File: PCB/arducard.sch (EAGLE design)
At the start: 54 parts, among them J1 USB MICRO, Q1 BC817-16LT1SMD, Q2 NTR0202PL, U1 microSD, U2 ATMEGA32U4-XUAU, U3 LM3658, Y1 16MHz KX-7

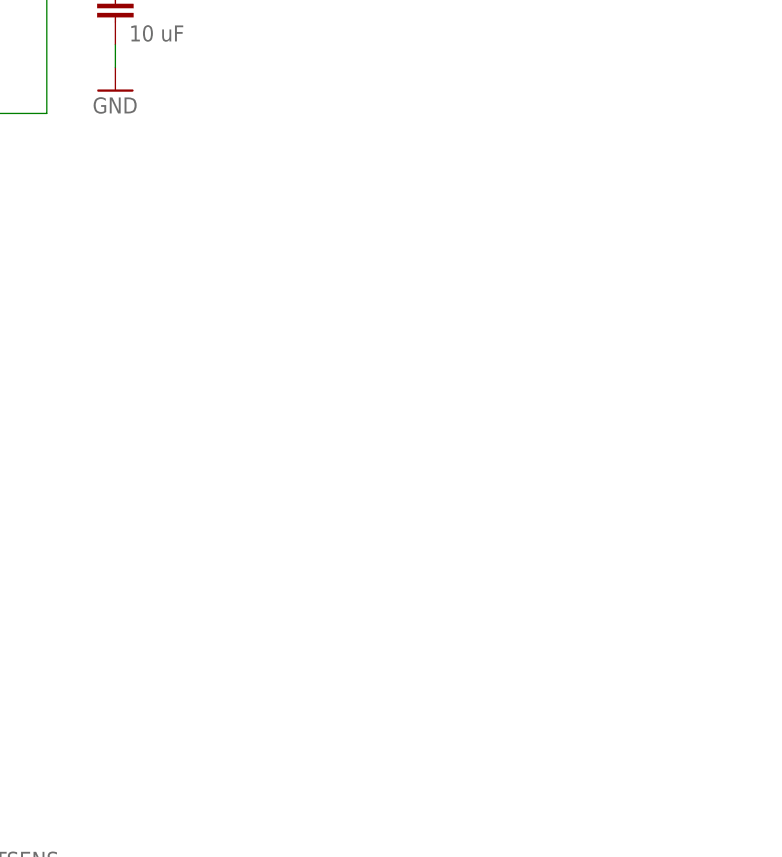
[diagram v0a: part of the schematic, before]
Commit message: Added DS3234 Real Time Clock
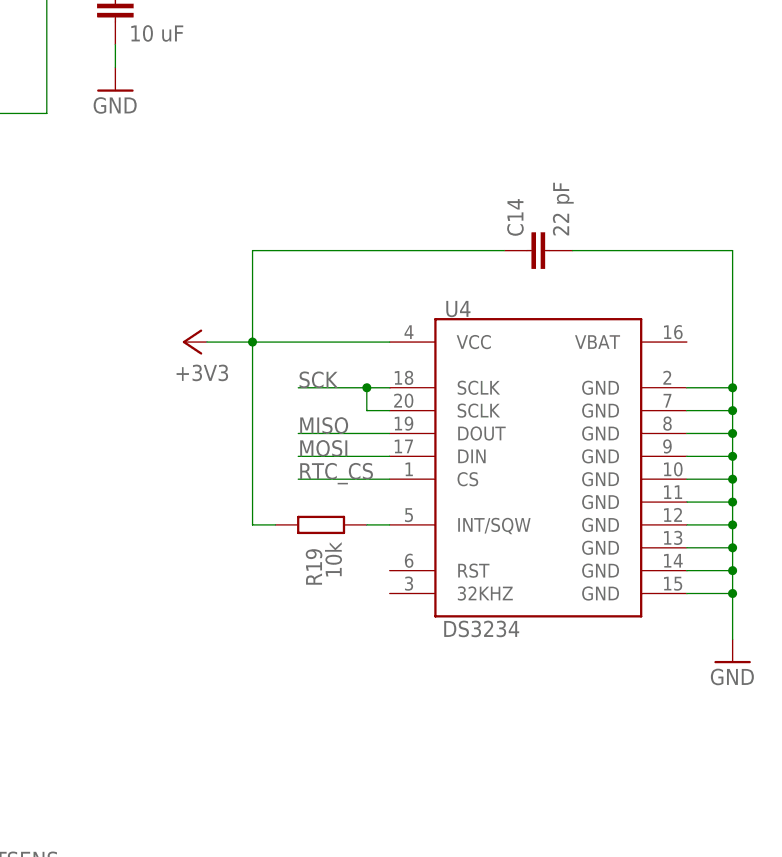
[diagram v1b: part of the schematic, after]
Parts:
- added C14: 22 pF, SmartPrj:C-EUC0603
- added R19: 10k, SmartPrj:R-EU_R0603
- added U4: DS3234, SparkFun:DS3234
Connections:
- new net N$17: R19.1, U4.INT/SQW
- new net RTC_CS: U4.CS
- net +3V3: now also C14.1, R19.2, U4.VCC
- net GND: now also C14.2, U4.GND, U4.GND@10, U4.GND@11, U4.GND@12, U4.GND@13, U4.GND@14, U4.GND@2, U4.GND@7, U4.GND@8, U4.GND@9
- net MISO: now also U4.DOUT
- net MOSI: now also U4.DIN
- net SCK: now also U4.SCLK@18, U4.SCLK@20
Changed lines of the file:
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@@
 <part name="R18" library="SmartPrj" deviceset="R-EU_" device="R0603" value="10k"/>
 <part name="GND14" library="supply1" deviceset="GND" device=""/>
+<part name="U4" library="SparkFun" deviceset="DS3234" device=""/>
+<part name="GND17" library="supply1" deviceset="GND" device=""/>
+<part name="+3V8" library="supply1" deviceset="+3V3" device=""/>
+<part name="R19" library="SmartPrj" deviceset="R-EU_" device="R0603" value="10k"/>
+<part name="C14" library="SmartPrj" deviceset="C-EU" device="C0603" value="22 pF"/>
 </parts>
 <sheets>
@@
 </instance>
 <instance part="GND14" gate="1" x="546.1" y="-5.08"/>
+<instance part="U4" gate="G$1" x="624.84" y="63.5"/>
+<instance part="GND17" gate="1" x="647.7" y="40.64"/>
+<instance part="+3V8" gate="G$1" x="586.74" y="76.2" rot="R90"/>
+<instance part="R19" gate="G$1" x="601.98" y="55.88" smashed="yes" rot="R180">
+<attribute name="NAME" x="600.3036" y="53.34" size="1.778" layer="95" rot="R270"/>
+<attribute name="VALUE" x="602.488" y="53.975" size="1.778" layer="96" rot="R270"/>
+</instance>
+<instance part="C14" gate="G$1" x="624.84" y="86.36" rot="R90"/>
 </instances>
 <busses>
@@
 <junction x="546.1" y="2.54"/>
 </segment>
+<segment>
+<pinref part="U4" gate="G$1" pin="GND@2"/>
+<wire x1="642.62" y1="71.12" x2="647.7" y2="71.12" width="0.1524" layer="91"/>
+<wire x1="647.7" y1="71.12" x2="647.7" y2="68.58" width="0.1524" layer="91"/>
+<pinref part="U4" gate="G$1" pin="GND@7"/>
+<wire x1="647.7" y1="68.58" x2="647.7" y2="66.04" width="0.1524" layer="91"/>
+<wire x1="647.7" y1="66.04" x2="647.7" y2="63.5" width="0.1524" layer="91"/>
+<wire x1="647.7" y1="63.5" x2="647.7" y2="60.96" width="0.1524" layer="91"/>
+<wire x1="647.7" y1="60.96" x2="647.7" y2="58.42" width="0.1524" layer="91"/>
+<wire x1="647.7" y1="58.42" x2="647.7" y2="55.88" width="0.1524" layer="91"/>
+<wire x1="647.7" y1="55.88" x2="647.7" y2="53.34" width="0.1524" layer="91"/>
+<wire x1="647.7" y1="53.34" x2="647.7" y2="50.8" width="0.1524" layer="91"/>
+<wire x1="647.7" y1="50.8" x2="647.7" y2="48.26" width="0.1524" layer="91"/>
+<wire x1="647.7" y1="48.26" x2="647.7" y2="43.18" width="0.1524" layer="91"/>
+<wire x1="642.62" y1="68.58" x2="647.7" y2="68.58" width="0.1524" layer="91"/>
+<pinref part="U4" gate="G$1" pin="GND@8"/>
+<wire x1="642.62" y1="66.04" x2="647.7" y2="66.04" width="0.1524" layer="91"/>
+<pinref part="U4" gate="G$1" pin="GND@9"/>
+<wire x1="642.62" y1="63.5" x2="647.7" y2="63.5" width="0.1524" layer="91"/>
+<pinref part="U4" gate="G$1" pin="GND@10"/>
+<wire x1="642.62" y1="60.96" x2="647.7" y2="60.96" width="0.1524" layer="91"/>
+<pinref part="U4" gate="G$1" pin="GND@11"/>
+<wire x1="642.62" y1="58.42" x2="647.7" y2="58.42" width="0.1524" layer="91"/>
+<pinref part="U4" gate="G$1" pin="GND@12"/>
+<wire x1="642.62" y1="55.88" x2="647.7" y2="55.88" width="0.1524" layer="91"/>
+<pinref part="U4" gate="G$1" pin="GND@13"/>
+<wire x1="642.62" y1="53.34" x2="647.7" y2="53.34" width="0.1524" layer="91"/>
+<pinref part="U4" gate="G$1" pin="GND@14"/>
+<wire x1="642.62" y1="50.8" x2="647.7" y2="50.8" width="0.1524" layer="91"/>
+<pinref part="U4" gate="G$1" pin="GND"/>
+<wire x1="642.62" y1="48.26" x2="647.7" y2="48.26" width="0.1524" layer="91"/>
+<junction x="647.7" y="48.26"/>
+<junction x="647.7" y="50.8"/>
+<junction x="647.7" y="53.34"/>
+<junction x="647.7" y="55.88"/>
+<junction x="647.7" y="58.42"/>
+<junction x="647.7" y="60.96"/>
+<junction x="647.7" y="63.5"/>
+<junction x="647.7" y="66.04"/>
+<junction x="647.7" y="68.58"/>
+<pinref part="GND17" gate="1" pin="GND"/>
+<pinref part="C14" gate="G$1" pin="2"/>
+<wire x1="629.92" y1="86.36" x2="647.7" y2="86.36" width="0.1524" layer="91"/>
+<wire x1="647.7" y1="86.36" x2="647.7" y2="71.12" width="0.1524" layer="91"/>
+<junction x="647.7" y="71.12"/>
+</segment>
 </net>
 <net name="RESET" class="0">
@@
 <label x="185.42" y="109.22" size="1.778" layer="95"/>
 </segment>
+<segment>
+<pinref part="U4" gate="G$1" pin="SCLK@18"/>
+<wire x1="609.6" y1="71.12" x2="607.06" y2="71.12" width="0.1524" layer="91"/>
+<pinref part="U4" gate="G$1" pin="SCLK@20"/>
+<wire x1="607.06" y1="71.12" x2="599.44" y2="71.12" width="0.1524" layer="91"/>
+<wire x1="609.6" y1="68.58" x2="607.06" y2="68.58" width="0.1524" layer="91"/>
+<wire x1="607.06" y1="68.58" x2="607.06" y2="71.12" width="0.1524" layer="91"/>
+<junction x="607.06" y="71.12"/>
+<label x="599.44" y="71.12" size="1.778" layer="95"/>
+</segment>
 </net>
 <net name="MISO" class="0">
@@
 <label x="185.42" y="114.3" size="1.778" layer="95"/>
 </segment>
+<segment>
+<pinref part="U4" gate="G$1" pin="DOUT"/>
+<wire x1="609.6" y1="66.04" x2="599.44" y2="66.04" width="0.1524" layer="91"/>
+<label x="599.44" y="66.04" size="1.778" layer="95"/>
+</segment>
 </net>
 <net name="MOSI" class="0">
@@
 <wire x1="172.72" y1="111.76" x2="185.42" y2="111.76" width="0.1524" layer="91"/>
 <label x="185.42" y="111.76" size="1.778" layer="95"/>
+</segment>
+<segment>
+<pinref part="U4" gate="G$1" pin="DIN"/>
+<wire x1="609.6" y1="63.5" x2="599.44" y2="63.5" width="0.1524" layer="91"/>
+<label x="599.44" y="63.5" size="1.778" layer="95"/>
 </segment>
 </net>
@@
 <junction x="236.22" y="208.28"/>
 </segment>
+<segment>
+<pinref part="+3V8" gate="G$1" pin="+3V3"/>
+<pinref part="U4" gate="G$1" pin="VCC"/>
+<wire x1="589.28" y1="76.2" x2="594.36" y2="76.2" width="0.1524" layer="91"/>
+<pinref part="R19" gate="G$1" pin="2"/>
+<wire x1="594.36" y1="76.2" x2="609.6" y2="76.2" width="0.1524" layer="91"/>
+<wire x1="596.9" y1="55.88" x2="594.36" y2="55.88" width="0.1524" layer="91"/>
+<wire x1="594.36" y1="55.88" x2="594.36" y2="76.2" width="0.1524" layer="91"/>
+<junction x="594.36" y="76.2"/>
+<wire x1="594.36" y1="76.2" x2="594.36" y2="86.36" width="0.1524" layer="91"/>
+<pinref part="C14" gate="G$1" pin="1"/>
+<wire x1="594.36" y1="86.36" x2="622.3" y2="86.36" width="0.1524" layer="91"/>
+</segment>
 </net>
 <net name="SRAM_CS" class="0">
@@
 </segment>
 </net>
+<net name="RTC_CS" class="0">
+<segment>
+<pinref part="U4" gate="G$1" pin="CS"/>
+<wire x1="609.6" y1="60.96" x2="599.44" y2="60.96" width="0.1524" layer="91"/>
+<label x="599.44" y="60.96" size="1.778" layer="95"/>
+</segment>
+</net>
+<net name="N$17" class="0">
+<segment>
+<pinref part="R19" gate="G$1" pin="1"/>
+<pinref part="U4" gate="G$1" pin="INT/SQW"/>
+<wire x1="607.06" y1="55.88" x2="609.6" y2="55.88" width="0.1524" layer="91"/>
+</segment>
+</net>

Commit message: Added display ZIF connector and control circuit
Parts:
- added C15, C16, C17, C18, C19, C20, C21, C22, C23, C24, C25, C27, C28, C29, C30: 2.2uF, SmartPrj:C-EUC0603
- added C26: 1uF, SmartPrj:C-EUC0603
- added C31: 100nF, SmartPrj:C-EUC0603
- added D1: BAT54S, diode:BAT54S
- added Q3, Q5, Q6: 2N7002, AWJLEagleLib:2N7002
- added Q4: BSS84, transistor-small-signal:BSS84
- added R20, R21: 2k, SmartPrj:R-EU_R0603
- added R22, R23, R24: 100k, SmartPrj:R-EU_R0603
- added U$2: 051296-4094, arducard-fpc:051296-4094
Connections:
- new net BORDER: Q3.D, R21.1, R22.2, U$2.BORDER
- new net BORDER_CONTROL: Q4.G
- new net DISCHARGE: Q5.G, Q6.G
- new net EPD_BUSY: U$2.BUSY
- new net EPD_CS: U$2.CSB
- new net EPD_RESET: U$2.RESETB
- new net N$1: C15.2, U$2.VCL
- new net N$12: C16.2, U$2.C42P
- new net N$14: C16.1, U$2.C42M
- new net N$15: C17.2, U$2.C41P
- new net N$16: C17.1, U$2.C41M
- new net N$18: C18.2, U$2.C31M
- new net N$19: C18.1, U$2.C31P
- new net N$20: C19.2, U$2.C21M
- new net N$21: C19.1, U$2.C21P
- new net N$22: C20.2, U$2.C16M
- new net N$23: C20.1, U$2.C16P
- new net N$24: C21.1, U$2.C15M
- new net N$25: C21.2, U$2.C15P
- new net N$26: C22.2, U$2.C14P
- new net N$27: C22.1, U$2.C14M
- new net N$28: C23.2, U$2.C13P
- new net N$29: C23.1, U$2.C13M
- new net N$30: C24.2, U$2.C12P
- new net N$31: C24.1, U$2.C12M
- new net N$32: C25.2, U$2.C11P
- new net N$33: C25.1, U$2.C11M
- new net N$38: Q4.D, R24.2
- new net N$39: Q3.G, R23.2, R24.1
- new net N$40: C31.1, D1.C1A2
- new net N$41: R21.2, U$2.ADC_IN
- new net PWM: C31.2
- new net VCOM: C26.2, R20.1, R22.1, U$2.VCOM_PANEL, U$2.VST
- new net VCOM_DRIVER: R20.2, U$2.VCOM_DRIVER
- new net VDH: C29.2, Q6.D, U$2.VDH
- new net VDL: C30.2, Q3.S, R23.1, U$2.VDL
- new net VGH: C27.2, Q5.D, U$2.VGH
- new net VGL: C28.2, D1.A1, U$2.VGL
- net +3V3: now also Q4.S, U$2.VCC, U$2.VDD
- net CDP: now also U1.CD2
- net GND: now also C15.1, C26.1, C27.1, C28.1, C29.1, C30.1, D1.C2, Q5.S, Q6.S, U$2.ID, U$2.VSS
- net MISO: now also U$2.SO
- net MOSI: now also U$2.SI
- net SCK: now also U$2.SCLK
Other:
- note added: "CHANGE ME"

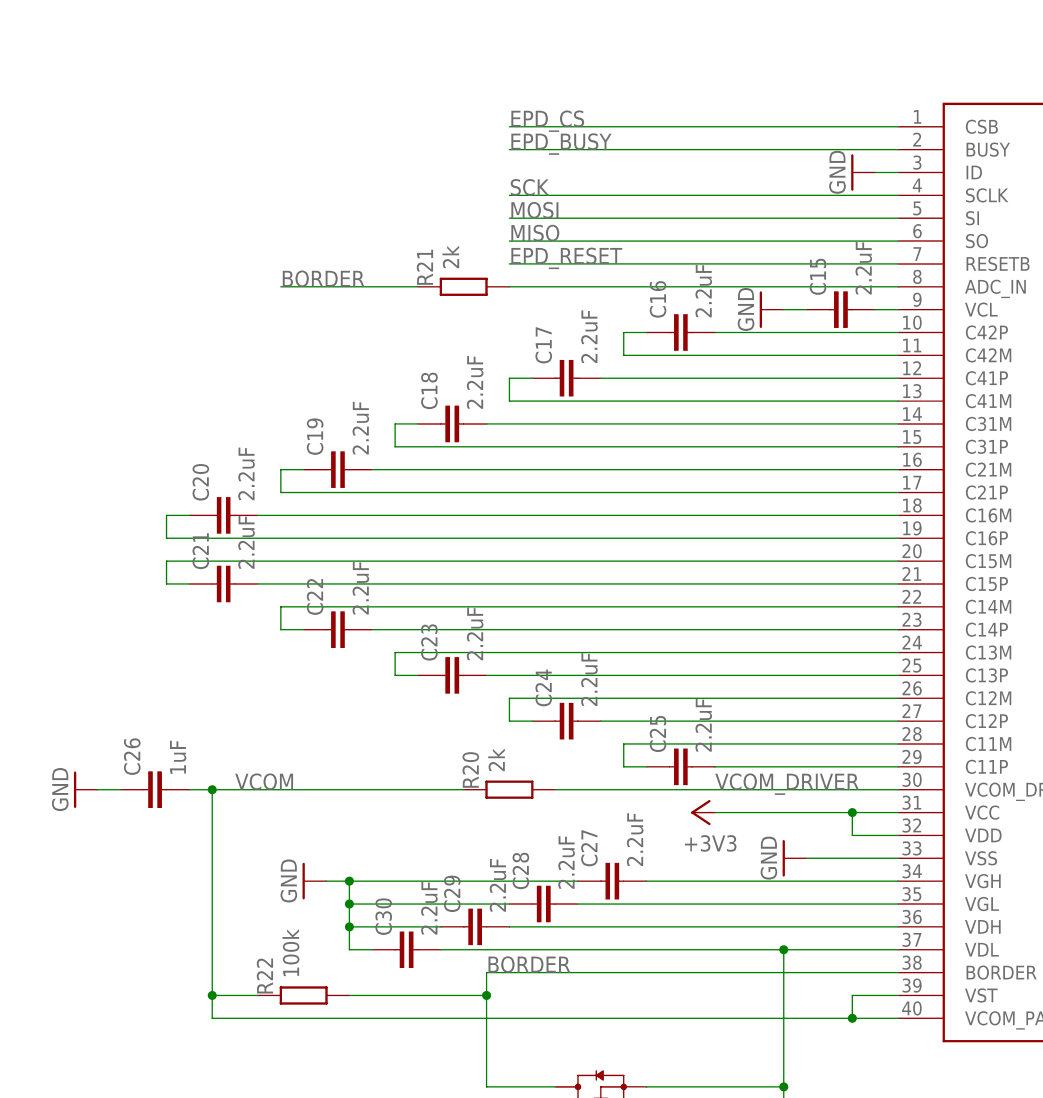
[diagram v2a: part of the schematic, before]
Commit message: Added voltage ratings to display control circuit
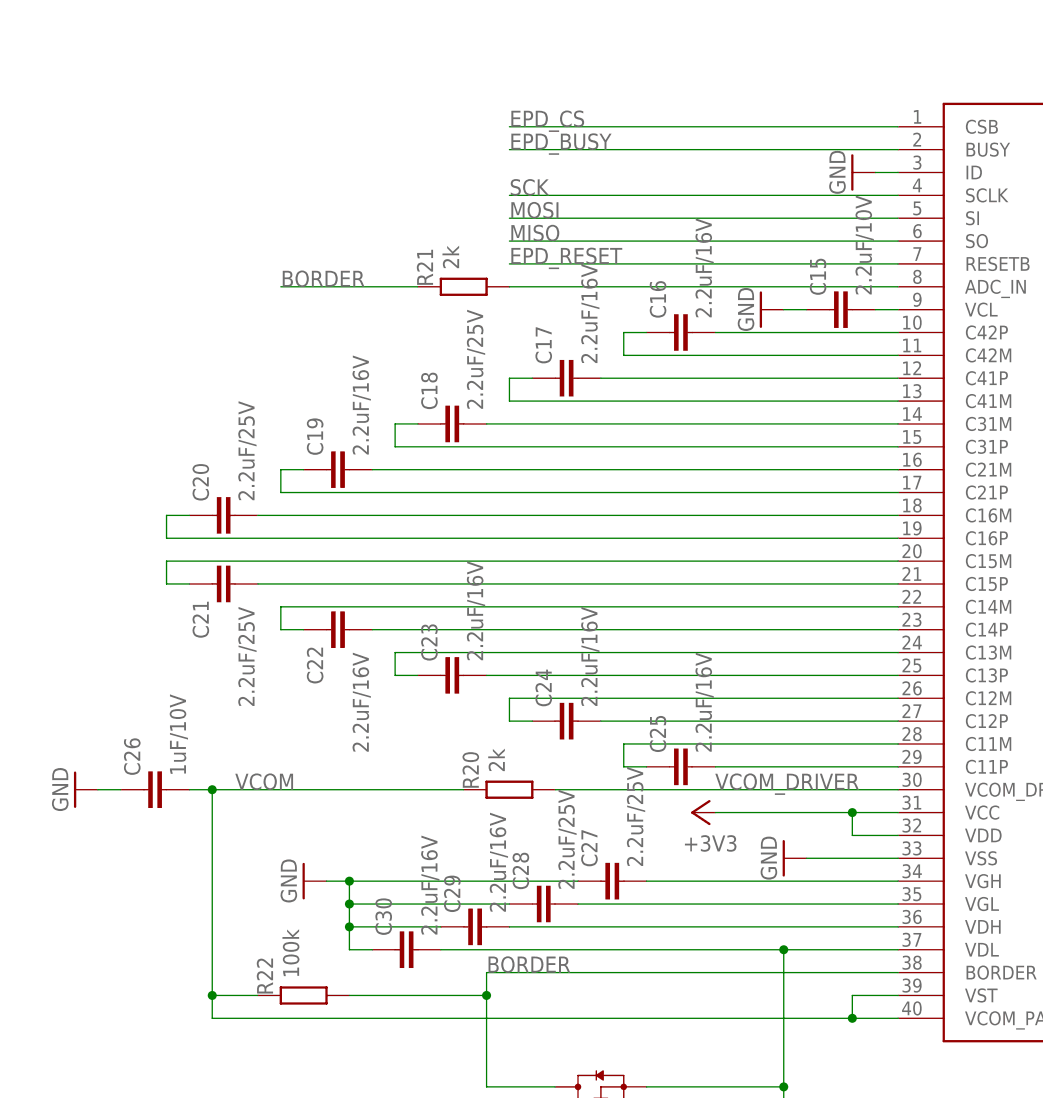
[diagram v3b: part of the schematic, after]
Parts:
- C15: value 2.2uF -> 2.2uF/10V
- C16, C17, C19, C22, C23, C24, C25, C29, C30: value 2.2uF -> 2.2uF/16V
- C18, C20, C21, C27, C28: value 2.2uF -> 2.2uF/25V
- C26: value 1uF -> 1uF/10V
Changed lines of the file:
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@@
 <part name="U$2" library="arducard-fpc" deviceset="051296-4094" device=""/>
 <part name="GND20" library="supply1" deviceset="GND" device=""/>
-<part name="C15" library="SmartPrj" deviceset="C-EU" device="C0603" value="2.2uF"/>
-<part name="C16" library="SmartPrj" deviceset="C-EU" device="C0603" value="2.2uF"/>
-<part name="C17" library="SmartPrj" deviceset="C-EU" device="C0603" value="2.2uF"/>
-<part name="C18" library="SmartPrj" deviceset="C-EU" device="C0603" value="2.2uF"/>
-<part name="C19" library="SmartPrj" deviceset="C-EU" device="C0603" value="2.2uF"/>
-<part name="C20" library="SmartPrj" deviceset="C-EU" device="C0603" value="2.2uF"/>
-<part name="C21" library="SmartPrj" deviceset="C-EU" device="C0603" value="2.2uF"/>
-<part name="C22" library="SmartPrj" deviceset="C-EU" device="C0603" value="2.2uF"/>
-<part name="C23" library="SmartPrj" deviceset="C-EU" device="C0603" value="2.2uF"/>
-<part name="C24" library="SmartPrj" deviceset="C-EU" device="C0603" value="2.2uF"/>
-<part name="C25" library="SmartPrj" deviceset="C-EU" device="C0603" value="2.2uF"/>
+<part name="C15" library="SmartPrj" deviceset="C-EU" device="C0603" value="2.2uF/10V"/>
+<part name="C16" library="SmartPrj" deviceset="C-EU" device="C0603" value="2.2uF/16V"/>
+<part name="C17" library="SmartPrj" deviceset="C-EU" device="C0603" value="2.2uF/16V"/>
+<part name="C18" library="SmartPrj" deviceset="C-EU" device="C0603" value="2.2uF/25V"/>
+<part name="C19" library="SmartPrj" deviceset="C-EU" device="C0603" value="2.2uF/16V"/>
+<part name="C20" library="SmartPrj" deviceset="C-EU" device="C0603" value="2.2uF/25V"/>
+<part name="C21" library="SmartPrj" deviceset="C-EU" device="C0603" value="2.2uF/25V"/>
+<part name="C22" library="SmartPrj" deviceset="C-EU" device="C0603" value="2.2uF/16V"/>
+<part name="C23" library="SmartPrj" deviceset="C-EU" device="C0603" value="2.2uF/16V"/>
+<part name="C24" library="SmartPrj" deviceset="C-EU" device="C0603" value="2.2uF/16V"/>
+<part name="C25" library="SmartPrj" deviceset="C-EU" device="C0603" value="2.2uF/16V"/>
 <part name="+3V9" library="supply1" deviceset="+3V3" device=""/>
 <part name="GND21" library="supply1" deviceset="GND" device=""/>
-<part name="C26" library="SmartPrj" deviceset="C-EU" device="C0603" value="1uF"/>
-<part name="C27" library="SmartPrj" deviceset="C-EU" device="C0603" value="2.2uF"/>
+<part name="C26" library="SmartPrj" deviceset="C-EU" device="C0603" value="1uF/10V"/>
+<part name="C27" library="SmartPrj" deviceset="C-EU" device="C0603" value="2.2uF/25V"/>
 <part name="GND22" library="supply1" deviceset="GND" device=""/>
-<part name="C28" library="SmartPrj" deviceset="C-EU" device="C0603" value="2.2uF"/>
-<part name="C29" library="SmartPrj" deviceset="C-EU" device="C0603" value="2.2uF"/>
-<part name="C30" library="SmartPrj" deviceset="C-EU" device="C0603" value="2.2uF"/>
+<part name="C28" library="SmartPrj" deviceset="C-EU" device="C0603" value="2.2uF/25V"/>
+<part name="C29" library="SmartPrj" deviceset="C-EU" device="C0603" value="2.2uF/16V"/>
+<part name="C30" library="SmartPrj" deviceset="C-EU" device="C0603" value="2.2uF/16V"/>
 <part name="R20" library="SmartPrj" deviceset="R-EU_" device="R0603" value="2k"/>
 <part name="GND26" library="supply1" deviceset="GND" device=""/>
@@
 <instance part="C19" gate="G$1" x="759.46" y="38.1" rot="R90"/>
 <instance part="C20" gate="G$1" x="746.76" y="33.02" rot="R90"/>
-<instance part="C21" gate="G$1" x="746.76" y="25.4" rot="R90"/>
-<instance part="C22" gate="G$1" x="759.46" y="20.32" rot="R90"/>
-<instance part="C23" gate="G$1" x="772.16" y="15.24" rot="R90"/>
+<instance part="C21" gate="G$1" x="746.76" y="25.4" smashed="yes" rot="R90">
+<attribute name="NAME" x="746.379" y="19.304" size="1.778" layer="95" rot="R90"/>
+<attribute name="VALUE" x="751.459" y="11.684" size="1.778" layer="96" rot="R90"/>
+</instance>
+<instance part="C22" gate="G$1" x="759.46" y="20.32" smashed="yes" rot="R90">
+<attribute name="NAME" x="759.079" y="14.224" size="1.778" layer="95" rot="R90"/>
+<attribute name="VALUE" x="764.159" y="6.604" size="1.778" layer="96" rot="R90"/>
+</instance>
+<instance part="C23" gate="G$1" x="772.16" y="15.24" smashed="yes" rot="R90">
+<attribute name="NAME" x="771.779" y="16.764" size="1.778" layer="95" rot="R90"/>
+<attribute name="VALUE" x="776.859" y="16.764" size="1.778" layer="96" rot="R90"/>
+</instance>
 <instance part="C24" gate="G$1" x="784.86" y="10.16" rot="R90"/>
 <instance part="C25" gate="G$1" x="797.56" y="5.08" rot="R90"/>
